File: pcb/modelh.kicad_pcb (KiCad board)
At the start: 4 copper layers, 150 x 38 mm, 16 parts, among them J1 Battery Conn, J2 Conn_01x16, J3 Conn_01x12, J4 Conn_01x04, U1 nice_nano, U2 74HC595, U3 74HC595

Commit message: version 0.2
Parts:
- added D1: D_Small, Library:DO-35 smaller, F.Cu at (104.8, 65.0)
- added D10: D_Small, Library:DO-35 smaller, F.Cu at (136.8, 65.0)
- added D11: D_Small, Library:DO-35 smaller, F.Cu at (140.3, 65.0)
- added D12: D_Small, Library:DO-35 smaller, F.Cu at (143.9, 65.0)
- added D13: D_Small, Library:DO-35 smaller, F.Cu at (147.4, 65.0)
- added D14: D_Small, Library:DO-35 smaller, F.Cu at (151.0, 65.0)
- added D15: D_Small, Library:DO-35 smaller, F.Cu at (154.5, 65.0)
- added D16: D_Small, Library:DO-35 smaller, F.Cu at (158.1, 65.0)
- added D2: D_Small, Library:DO-35 smaller, F.Cu at (108.4, 65.0)
- added D3: D_Small, Library:DO-35 smaller, F.Cu at (111.9, 65.0)
- added D4: D_Small, Library:DO-35 smaller, F.Cu at (115.5, 65.0)
- added D5: D_Small, Library:DO-35 smaller, F.Cu at (119.0, 65.0)
- added D6: D_Small, Library:DO-35 smaller, F.Cu at (122.6, 65.0)
- added D7: D_Small, Library:DO-35 smaller, F.Cu at (126.1, 65.0)
- added D8: D_Small, Library:DO-35 smaller, F.Cu at (129.7, 65.0)
- added D9: D_Small, Library:DO-35 smaller, F.Cu at (133.2, 65.0)
- added G***: LOGO, Library:fr, F.Cu at (213.6, 70.2)
- added J5: Conn_01x06, Connector_PinHeader_2.54mm:PinHeader_1x06_P2.54mm_Vertical, F.Cu at (68.3, 82.6)
- added REF**: OSHW-Logo2_7.3x6mm_SilkScreen, Symbol:OSHW-Logo2_7.3x6mm_SilkScreen, F.Cu at (69.8, 51.5)
- moved R7 94.1 mm to (212.2, 54.9), turned to -90 degrees
- moved R8 90.2 mm to (209.0, 54.9), turned to -90 degrees
- moved R9 86.4 mm to (205.8, 54.9), turned to -90 degrees
- moved G*** 47.5 mm to (162.4, 30.6)
- moved J1 16.8 mm to (150.3, 78.5)
- moved U2 13.3 mm to (102.9, 78.8)
- moved U3 13.0 mm to (127.2, 78.8)
- moved JP5 0.82 mm to (99.8, 59.0)
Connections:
- J2 pad 1: col0 -> Net-(D1-K)
- J2 pad 10: col9 -> Net-(D10-K)
- J2 pad 11: col10 -> Net-(D11-K)
- J2 pad 12: col11 -> Net-(D12-K)
- J2 pad 13: col12 -> Net-(D13-K)
- J2 pad 14: col13 -> Net-(D14-K)
- J2 pad 15: col14 -> Net-(D15-K)
- J2 pad 16: col15 -> Net-(D16-K)
- J2 pad 2: col1 -> Net-(D2-K)
- J2 pad 3: col2 -> Net-(D3-K)
- J2 pad 4: col3 -> Net-(D4-K)
- J2 pad 5: col4 -> Net-(D5-K)
- J2 pad 6: col5 -> Net-(D6-K)
- J2 pad 7: col6 -> Net-(D7-K)
- J2 pad 8: col7 -> Net-(D8-K)
- J2 pad 9: col8 -> Net-(D9-K)
- JP5 pad 2: +3.3V -> GND
- U1 pad 10: unconnected-(U1-100-Pad10) -> user4
- U1 pad 2: SCLK -> user1
- U1 pad 3: CS -> user2
- U1 pad 7: unconnected-(U1-020-Pad7) -> SCLK
- U1 pad 8: unconnected-(U1-022-Pad8) -> CS
- U1 pad 9: unconnected-(U1-024-Pad9) -> user3
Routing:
- net led0: track 30.9 -> 140.4 mm
- net +3.3V: track 3.89 -> 111.8 mm
- net led1: track 31.1 -> 137.4 mm
- net led2: track 31.4 -> 134.4 mm
- net Net-(J3-Pin_9): track 101.9 -> 31.5 mm
- net Net-(J3-Pin_11): track 94.1 -> 28.9 mm
- net Net-(J3-Pin_12): track 89.0 -> 30.8 mm
- net user1: track 0.00 -> 34.5 mm
- net user2: track 0.00 -> 30.9 mm
- net user3: track 0.00 -> 16.0 mm
- net +BATT: track 80.8 -> 95.0 mm
- net user4: track 0.00 -> 13.3 mm
- net Net-(D16-K): track 0.00 -> 11.9 mm
- net Net-(D15-K): track 0.00 -> 11.0 mm
- net Net-(D14-K): track 0.00 -> 9.69 mm
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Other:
- rule pad_to_mask_clearance: 0.0508 -> 0
- board text added: "42x27mm Reserved for Li-Po battery"
- board text added: "User"
- board text added: "rusz.space/modelk"
- board text removed: "54x28mm Reserved for Li-Po battery"
- board text removed: "https://rusz.space/modelk"

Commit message: Added license
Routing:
- net SCLK: vias 1 -> 0
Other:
- board text added: "Copyright 2025 Filip Rusz; Licensed under BSD-3-Clause"

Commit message: Rev 0.3
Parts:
- removed REF**: OSHW-Logo2_7.3x6mm_SilkScreen, Symbol:OSHW-Logo2_7.3x6mm_SilkScreen
- added D17: D_Small, Library:D_SOD-123F-nicer, F.Cu at (147.3, 58.3)
- added D18: D_Small, Library:D_SOD-123F-nicer, F.Cu at (149.9, 60.8)
- added D19: D_Small, Library:D_SOD-123F-nicer, F.Cu at (152.4, 58.3)
- added D20: D_Small, Library:D_SOD-123F-nicer, F.Cu at (154.9, 60.8)
- added U4: 74HC595, Package_DIP:DIP-16_W7.62mm_Socket_LongPads, F.Cu at (167.6, 66.0)
- D1, D10, D11, D12, D13, D14, D15, D16, D2, D3, D4, D5, D6, D7, D8, D9: footprint Library:DO-35 smaller -> Library:D_SOD-123F-nicer
- J2: value Conn_01x16 -> Conn_01x20; footprint Library:ModelH-triomate-cols16 -> Library:ModelH-triomate-cols20
- moved R9 92.6 mm to (116.8, 80.6), turned to 180 degrees
- moved R8 81.1 mm to (132.1, 80.6), turned to 180 degrees
- moved R7 69.8 mm to (147.3, 80.6), turned to 180 degrees
- moved J5 31.2 mm to (68.2, 51.4), turned to 0 degrees
- moved U2 24.0 mm to (123.2, 66.0), turned to -90 degrees
- moved U3 22.2 mm to (145.4, 66.0), turned to -90 degrees
- moved J1 20.6 mm to (160.1, 60.4)
- moved G*** 19.0 mm to (200.3, 83.8), turned to 0 degrees
- moved D15 14.0 mm to (142.2, 58.3), turned to -90 degrees
- moved D16 13.9 mm to (144.8, 60.8), turned to -90 degrees
- moved D13 12.3 mm to (137.2, 58.3), turned to -90 degrees
- moved D14 12.0 mm to (139.7, 60.8), turned to -90 degrees
- moved D11 10.6 mm to (132.1, 58.3), turned to -90 degrees
- moved G*** 10.2 mm to (172.7, 30.1)
- moved D12 10.1 mm to (134.6, 60.8), turned to -90 degrees
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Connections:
- U2 pad 1: col1 -> col6
- U2 pad 15: col0 -> col7
- U2 pad 2: col2 -> col5
- U2 pad 3: col3 -> col4
- U2 pad 4: col4 -> col3
- U2 pad 5: col5 -> col2
- U2 pad 6: col6 -> col1
- U2 pad 7: col7 -> col0
- U3 pad 1: col9 -> col14
- U3 pad 15: col8 -> col15
- U3 pad 2: col10 -> col13
- U3 pad 3: col11 -> col12
- U3 pad 4: col12 -> col11
- U3 pad 5: col13 -> col10
- U3 pad 6: col14 -> col9
- U3 pad 7: col15 -> col8
- U3 pad 9: unconnected-(U3-QH&apos;-Pad9) -> Net-(U3-QH')
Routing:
- net led2: track 134.4 -> 28.2 mm
- net led1: track 137.4 -> 43.4 mm
- net led0: track 140.4 -> 58.7 mm
- net Net-(J3-Pin_9): track 31.5 -> 111.9 mm
- net Net-(J3-Pin_11): track 28.9 -> 88.0 mm
- net GND: track 0.00 -> 41.4 mm, vias 8 -> 4
- net Net-(U3-QH'): track 0.00 -> 39.3 mm
- net Net-(J3-Pin_12): track 30.8 -> 67.8 mm
- net +BATT: track 95.0 -> 66.7 mm
- net col16: track 0.00 -> 28.0 mm
- net Net-(U2-QH'): track 13.5 -> 37.8 mm
- net row4: track 85.5 -> 104.6 mm
- net user1: track 34.5 -> 16.0 mm
- net col13: track 22.3 -> 5.13 mm
- net col11: track 21.3 -> 5.13 mm
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- removed copper zone on In1.Cu, net GND
- removed copper zone on In2.Cu, net GND
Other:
- copper layers 4 -> 2
- board text added: "40x19mm Reserved for Li-Po battery"
- board text added: "Revision ${REVISION} issued ${ISSUE_DATE}"
- board text added: "https://rusz.space/modelk"
- board text removed: "42x27mm Reserved for Li-Po battery"
- board text removed: "REVISION ${REVISION} ISSUED ${ISSUE_DATE}"
- board text removed: "rusz.space/modelk"

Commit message: Small edits
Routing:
- net GND: track 41.4 -> 76.9 mm, vias 4 -> 5
- net +3.3V: track 106.9 -> 111.1 mm
- net CS: track 85.4 -> 86.6 mm
- net col16: track 28.0 -> 28.9 mm
- net MOSI: track 42.2 -> 43.0 mm
- net col19: track 4.87 -> 5.62 mm
- net col15: track 14.3 -> 14.9 mm
- net col9: track 5.13 -> 5.68 mm
- net col11: track 5.13 -> 5.63 mm
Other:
- board text removed: "S/N"

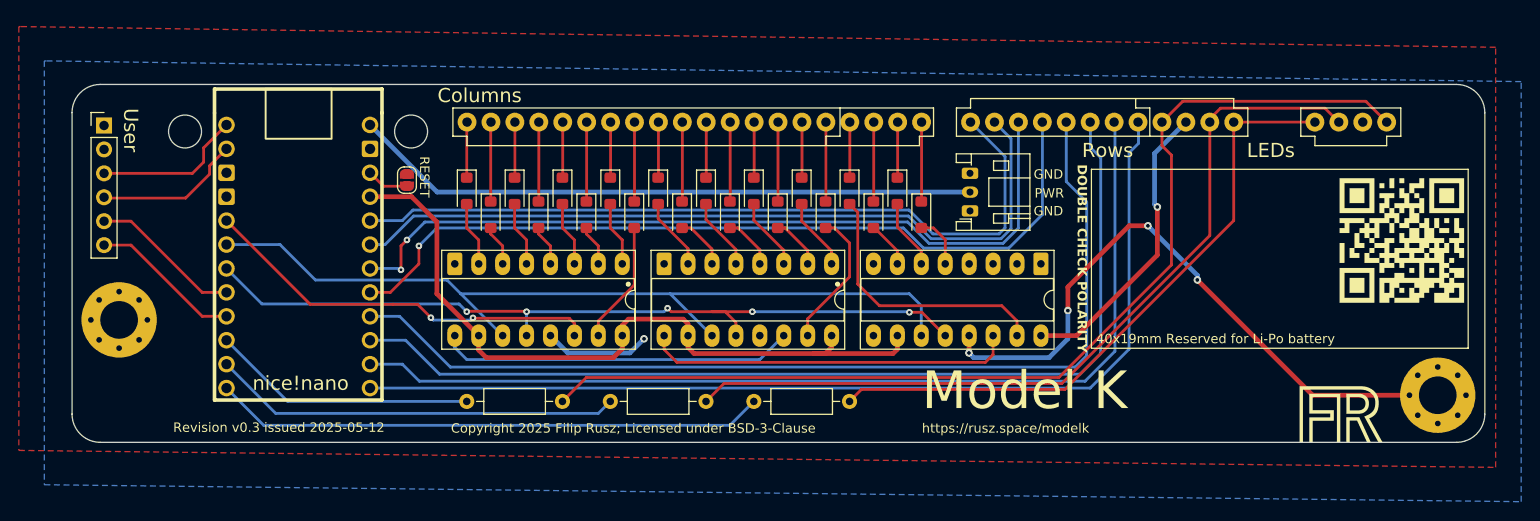
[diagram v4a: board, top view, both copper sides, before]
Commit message: Make it compatable with old pro micro
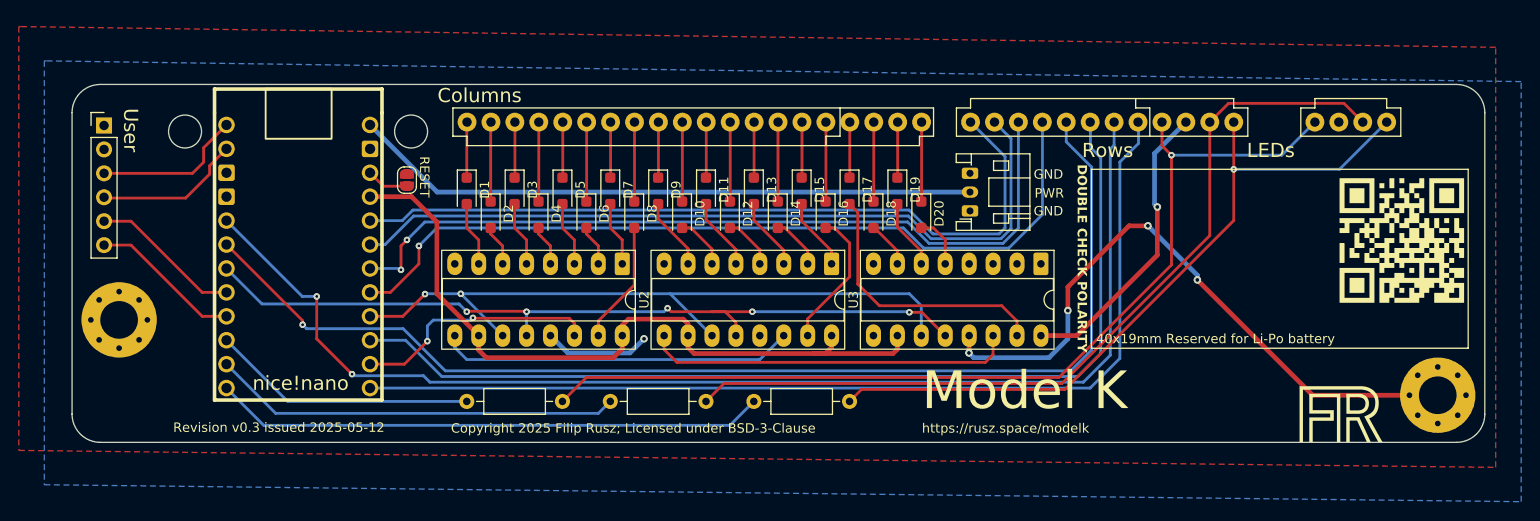
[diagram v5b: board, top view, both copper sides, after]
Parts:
- D1, D10, D11, D12, D13, D14, D15, D16, D17, D18, D19, D2, D20, D3, D4, D5, D6, D7, D8, D9: footprint Library:D_SOD-123F-nicer -> Diode_SMD:D_SOD-123F
- U2, U3: footprint PCM_Package_DIP_AKL:DIP-16_W7.62mm_Socket_LongPads -> Package_DIP:DIP-16_W7.62mm_Socket_LongPads
- turned J4 to 180 degrees
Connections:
- U1 pad 23: row4 -> SCLK
- U1 pad 25: row6 -> MOSI
- U1 pad 6: MOSI -> row6
- U1 pad 7: SCLK -> row4
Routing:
- net row6: track 105.5 -> 129.7 mm, vias 0 -> 2
- net row4: track 104.5 -> 123.9 mm, vias 0 -> 1
- net MOSI: track 43.0 -> 26.2 mm
- net SCLK: track 92.2 -> 75.8 mm, vias 0 -> 2
- net Net-(J3-Pin_12): track 67.8 -> 77.5 mm, vias 0 -> 1
- net Net-(J3-Pin_9): track 111.9 -> 102.9 mm, vias 0 -> 1
- net Net-(J3-Pin_11): track 88.0 -> 90.7 mm

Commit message: v3.1; made it uncompatible because HF pins
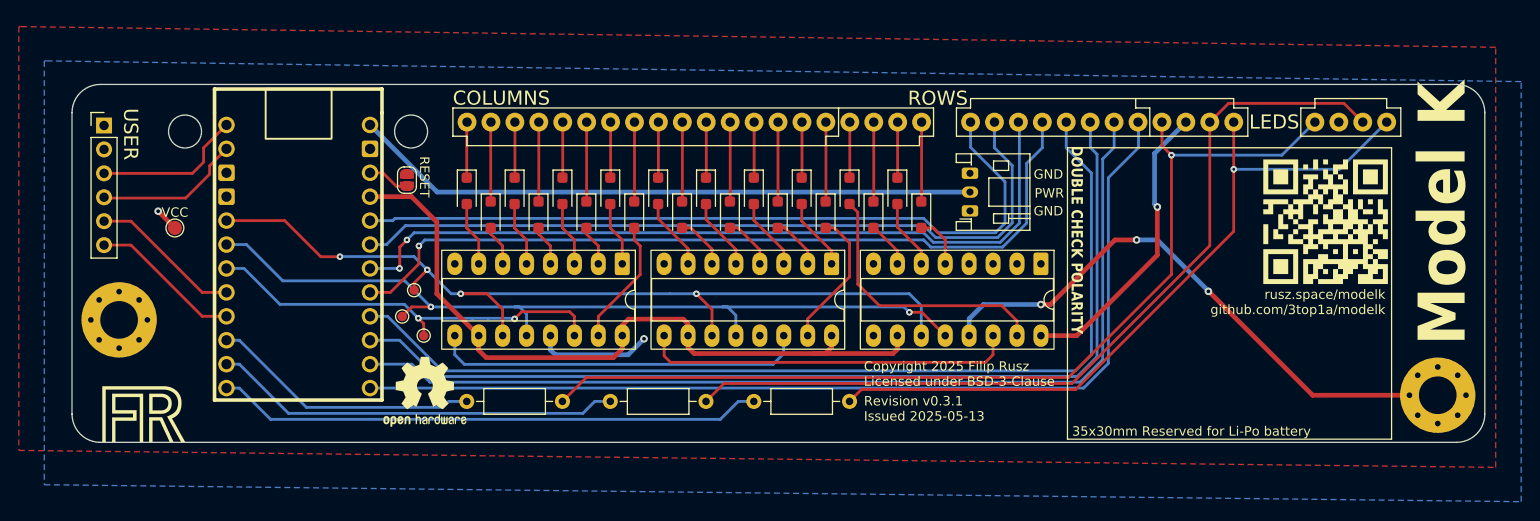
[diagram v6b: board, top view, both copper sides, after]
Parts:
- added CLK: SCLK, TestPoint:TestPoint_Pad_D1.0mm, F.Cu at (101.1, 68.8)
- added CS: CS, TestPoint:TestPoint_Pad_D1.0mm, F.Cu at (99.8, 71.6)
- added MOSI: MOSI, TestPoint:TestPoint_Pad_D1.0mm, F.Cu at (102.1, 73.7)
- added REF**: OSHW-Logo2_9.8x8mm_SilkScreen, Symbol:OSHW-Logo2_9.8x8mm_SilkScreen, F.Cu at (102.2, 79.6)
- added VCC: +, TestPoint:TestPoint_Pad_D1.5mm, F.Cu at (75.7, 62.2)
- moved G*** 127.1 mm to (73.2, 83.8)
- moved G*** 8.34 mm to (164.6, 28.1)
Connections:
- U1 pad 23: SCLK -> row4
- U1 pad 25: MOSI -> row6
- U1 pad 6: row6 -> SCLK
- U1 pad 7: row4 -> CS
- U1 pad 8: CS -> MOSI
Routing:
- net row6: track 129.7 -> 105.3 mm, vias 2 -> 0
- net SCLK: track 75.8 -> 96.5 mm, vias 2 -> 4
- net row4: track 123.9 -> 105.5 mm, vias 1 -> 0
- net MOSI: track 26.2 -> 43.5 mm
- net GND: track 76.9 -> 71.2 mm, vias 5 -> 4
- net CS: track 86.6 -> 91.6 mm, vias 5 -> 2
- net +3.3V: track 111.1 -> 113.7 mm, vias 1 -> 2
- net Net-(U2-QH'): track 37.8 -> 39.8 mm
- net row3: track 87.5 -> 85.9 mm
- net row2: track 85.3 -> 83.9 mm
- net row0: track 82.0 -> 80.8 mm
- net row1: track 82.8 -> 81.7 mm
- net Net-(J3-Pin_12): track 77.5 -> 78.2 mm
- net Net-(J3-Pin_11): track 90.7 -> 91.3 mm
- net Net-(J3-Pin_9): track 102.9 -> 103.5 mm
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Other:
- board text added: "35x30mm Reserved for Li-Po battery"
- board text added: "COLUMNS"
- board text added: "Copyright 2025 Filip Rusz Licensed under BSD-3-Clause"
- board text added: "LEDS"
- board text added: "ROWS"
- board text added: "Revision ${REVISION} Issued ${ISSUE_DATE}"
- board text added: "USER"
- board text added: "rusz.space/modelk github.com/3top1a/modelk"
- board text removed: "40x19mm Reserved for Li-Po battery"
- board text removed: "Columns"
- board text removed: "Copyright 2025 Filip Rusz; Licensed under BSD-3-Clause"
- board text removed: "LEDs"
- board text removed: "Revision ${REVISION} issued ${ISSUE_DATE}"
- board text removed: "Rows"
- board text removed: "User"
- board text removed: "https://rusz.space/modelk"

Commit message: Added actual reset switch
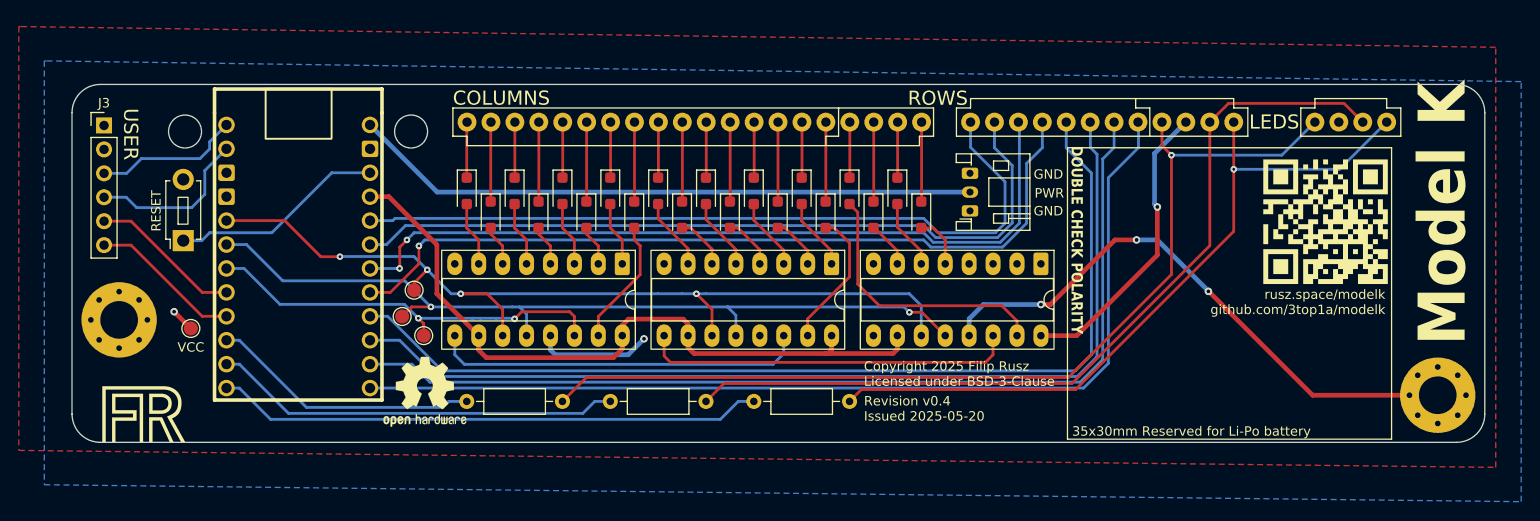
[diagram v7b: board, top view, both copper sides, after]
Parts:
- removed JP5: Reset jumper, Jumper:SolderJumper-2_P1.3mm_Open_RoundedPad1.0x1.5mm
- added SW1: SW_reset, Button_Switch_THT:SW_PUSH_1P1T_6x3.5mm_H4.3_APEM_MJTP1243, F.Cu at (76.6, 63.6)
- TP1: renamed from VCC; value + -> VCC; footprint TestPoint:TestPoint_Pad_D1.5mm -> Library:TestPoint
- TP2: renamed from MOSI; footprint TestPoint:TestPoint_Pad_D1.0mm -> Library:TestPoint
- TP3: renamed from CLK; footprint TestPoint:TestPoint_Pad_D1.0mm -> Library:TestPoint
- TP4: renamed from CS; footprint TestPoint:TestPoint_Pad_D1.0mm -> Library:TestPoint
- moved TP1 10.8 mm to (77.4, 72.9)
- renumbered J5 to J3, J3 to J4, J4 to J5, R7 to R1, R8 to R2, R9 to R3
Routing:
- net Net-(U1-RST): track 4.51 -> 22.8 mm
- net +3.3V: track 113.7 -> 111.2 mm
- net user2: track 15.7 -> 17.5 mm
- net CS: track 91.6 -> 90.6 mm

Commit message: Aligned connectors correctly, added second 4 pin footprint
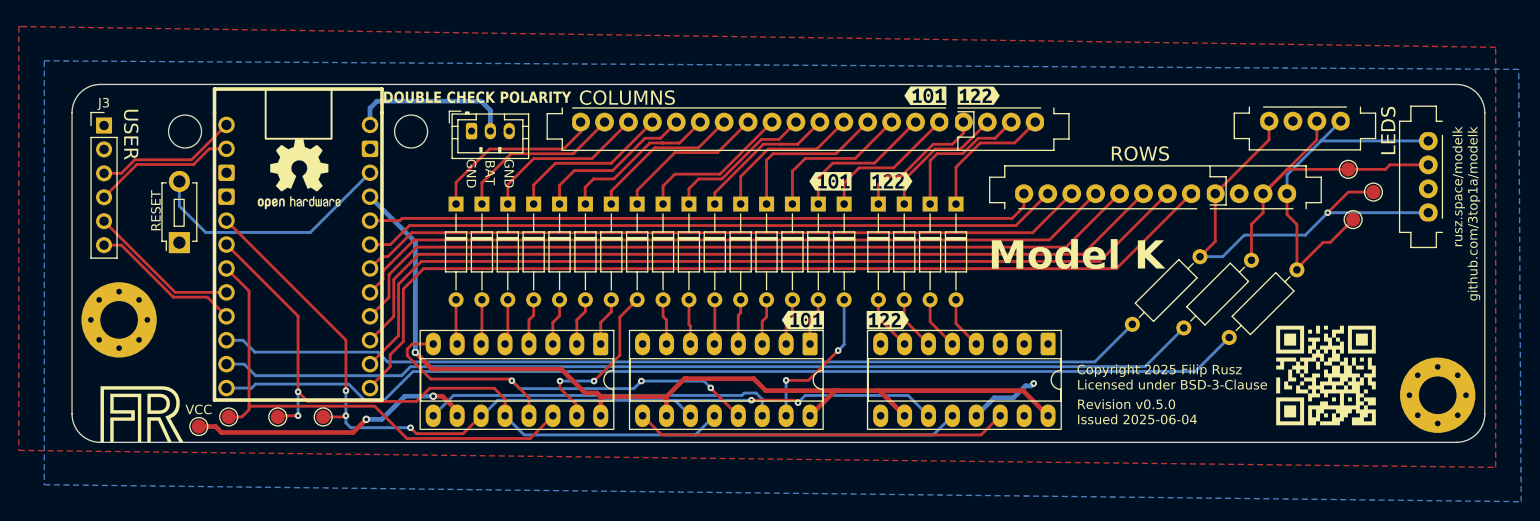
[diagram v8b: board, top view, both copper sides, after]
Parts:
- added J6: Conn_01x04, Library:ModelH-triomate-leds4, F.Cu at (195.7, 50.9)
- added TP5: LED1, Library:TestPoint, F.Cu at (200.8, 61.3)
- added TP6: LED2, Library:TestPoint, F.Cu at (200.3, 56.0)
- added TP7: LED3, Library:TestPoint, F.Cu at (202.9, 58.4)
- added kibuzzard-6839B796: G***, kibuzzard-6839B796, F.Cu at (151.4, 72.0)
- added kibuzzard-6839B796: G***, kibuzzard-6839B796, F.Cu at (161.0, 48.2)
- added kibuzzard-6839B796: G***, kibuzzard-6839B796, F.Cu at (151.8, 57.3)
- added kibuzzard-6839B7A3: G***, kibuzzard-6839B7A3, F.Cu at (155.4, 48.2)
- added kibuzzard-6839B7A3: G***, kibuzzard-6839B7A3, F.Cu at (142.4, 72.0)
- added kibuzzard-6839B7A3: G***, kibuzzard-6839B7A3, F.Cu at (145.3, 57.3)
- D1, D10, D11, D12, D13, D14, D15, D16, D17, D18, D19, D2, D20, D3, D4, D5, D6, D7, D8, D9: footprint Diode_SMD:D_SOD-123F -> Library:DO-35 smaller
- J1: footprint Connector_JST:JST_PH_S3B-PH-K_1x03_P2.00mm_Horizontal -> Connector_JST:JST_PH_B3B-PH-K_1x03_P2.00mm_Vertical
- moved R3 69.4 mm to (184.5, 65.3), turned to -135 degrees
- moved R2 59.8 mm to (190.0, 65.7), turned to -135 degrees
- moved J1 53.6 mm to (107.2, 51.9), turned to 0 degrees
- moved R1 49.5 mm to (194.8, 66.7), turned to -135 degrees
- moved REF** 26.7 mm to (88.9, 56.5)
- moved TP2 22.4 mm to (81.4, 82.3), turned to 90 degrees
- moved TP4 17.0 mm to (86.6, 82.3), turned to 90 degrees
- moved TP3 16.6 mm to (91.4, 82.3), turned to 90 degrees
- moved G*** 16.3 mm to (164.6, 44.4)
- moved J2 12.1 mm to (137.8, 51.0)
- moved TP1 10.4 mm to (78.2, 83.3)
- moved J5 10.1 mm to (208.8, 56.8), turned to -90 degrees
- moved J4 9.48 mm to (179.8, 57.6)
- moved U2 8.81 mm to (120.9, 74.5)
- moved U3 8.81 mm to (143.1, 74.5)
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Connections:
- net Net-(J4-Pin_11) renamed led1r
- net Net-(J4-Pin_12) renamed led0r
- net Net-(J4-Pin_9) renamed led2r
- SW1 pad 1: Net-(U1-RST) -> GND
- SW1 pad 2: GND -> Net-(U1-RST)
- U4 pad 15: col16 -> unconnected-(U4-QA-Pad15)
- U4 pad 4: unconnected-(U4-QE-Pad4) -> col19
- U4 pad 5: col19 -> col18
- U4 pad 6: col18 -> col17
- U4 pad 7: col17 -> col16
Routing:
- net led2: track 28.7 -> 98.8 mm
- net led1: track 43.4 -> 104.2 mm
- net led1r: track 91.3 -> 36.5 mm
- net led2r: track 103.5 -> 49.4 mm
- net led0: track 58.2 -> 110.2 mm
- net +BATT: track 66.7 -> 17.5 mm
- net led0r: track 78.2 -> 38.1 mm, vias 1 -> 0
- net col16: track 28.9 -> 5.85 mm
- net +3.3V: track 111.2 -> 132.8 mm, vias 2 -> 3
- net row4: track 105.5 -> 86.4 mm
- net GND: track 71.2 -> 54.1 mm
- net row5: track 104.9 -> 90.9 mm
- net Net-(D1-K): track 5.91 -> 18.8 mm
- net Net-(D3-K): track 5.91 -> 17.6 mm
- net Net-(D5-K): track 5.91 -> 17.2 mm
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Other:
- board text added: "BAT"
- board text added: "TODO:"
- board text removed: "35x30mm Reserved for Li-Po battery"
- board text removed: "PWR"
